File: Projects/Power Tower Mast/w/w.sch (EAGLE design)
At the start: 25 parts

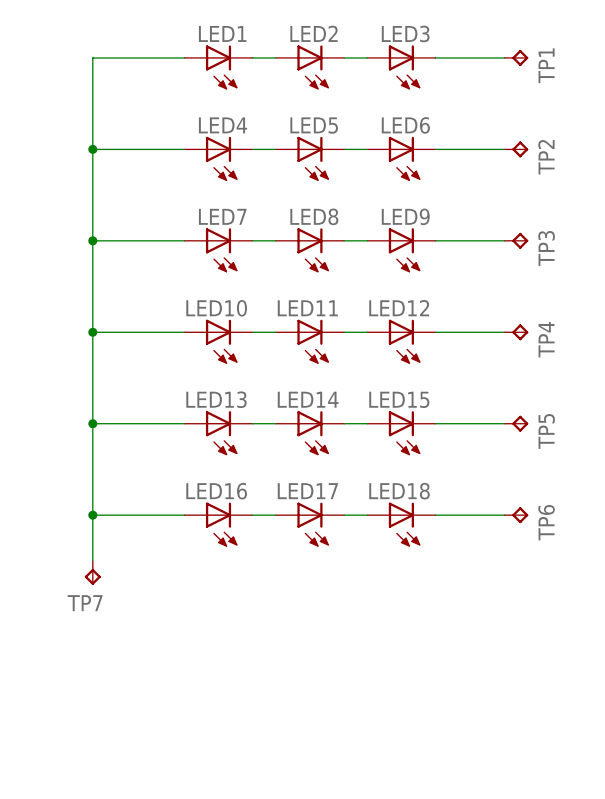
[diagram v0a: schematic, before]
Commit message: updated with extra vias and panelized
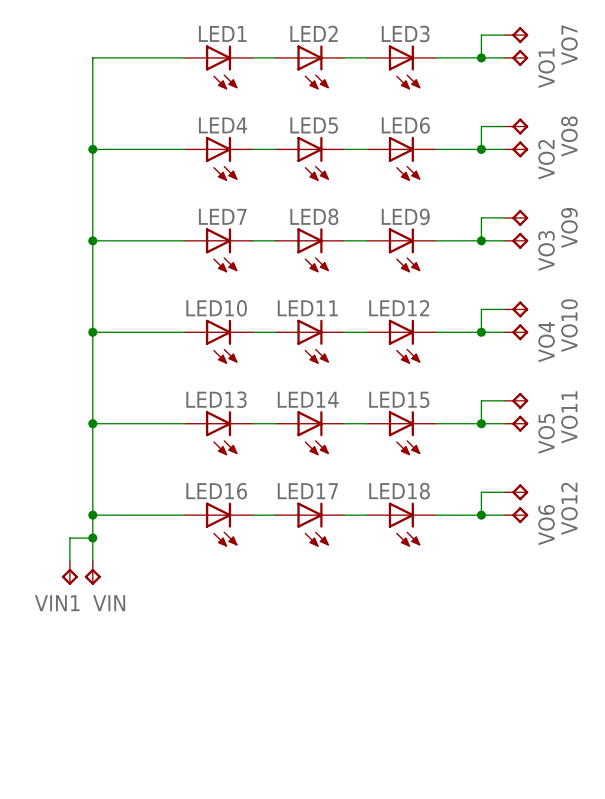
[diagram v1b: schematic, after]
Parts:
- added VIN1, VO10, VO11, VO12, VO7, VO8, VO9: (no value), CyberRailGuru:TEST_POINTPAD1-20
- renumbered TP1 to VO1, TP2 to VO2, TP3 to VO3, TP4 to VO4, TP5 to VO5, TP6 to VO6, TP7 to VIN
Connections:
- removed net VIN3: LED1.A, LED10.A, LED13.A, LED16.A, LED4.A, LED7.A, VIN.TP
- removed net VOUT14: LED3.C, VO1.TP
- removed net VOUT15: LED6.C, VO2.TP
- removed net VOUT16: LED9.C, VO3.TP
- removed net VOUT17: LED12.C, VO4.TP
- removed net VOUT18: LED15.C, VO5.TP
- removed net VOUT19: LED18.C, VO6.TP
- new net VIN: LED1.A, LED10.A, LED13.A, LED16.A, LED4.A, LED7.A, VIN.TP, VIN1.TP
- new net VOUT1: LED3.C, VO1.TP, VO7.TP
- new net VOUT2: LED6.C, VO2.TP, VO8.TP
- new net VOUT3: LED9.C, VO3.TP, VO9.TP
- new net VOUT4: LED12.C, VO10.TP, VO4.TP
- new net VOUT5: LED15.C, VO11.TP, VO5.TP
- new net VOUT6: LED18.C, VO12.TP, VO6.TP

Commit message: fixed ratio for all letters; continued to update layouts
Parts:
- added LED19, LED20, LED21: (no value), CyberRailGuru:LED0805
- added VO13, VO14: (no value), CyberRailGuru:TEST_POINTPAD1-20
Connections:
- new net N$1: LED19.C, LED20.A
- new net N$2: LED20.C, LED21.A
- new net VOUT7: LED21.C, VO14.TP, VO7.TP
- net VIN: now also LED19.A
- net VOUT1: now also VO8.TP; no longer VO7.TP
- net VOUT2: now also VO9.TP; no longer VO8.TP
- net VOUT3: now also VO10.TP; no longer VO9.TP
- net VOUT4: now also VO11.TP; no longer VO10.TP
- net VOUT5: now also VO12.TP; no longer VO11.TP
- net VOUT6: now also VO13.TP; no longer VO12.TP
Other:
- moved on the sheet: VIN, VIN1, VO10, VO11, VO12, VO7, VO8, VO9
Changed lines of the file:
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@@
 <part name="VO6" library="CyberRailGuru" deviceset="TEST_POINT" device="PAD1-20"/>
 <part name="VIN1" library="CyberRailGuru" deviceset="TEST_POINT" device="PAD1-20"/>
-<part name="VO7" library="CyberRailGuru" deviceset="TEST_POINT" device="PAD1-20"/>
 <part name="VO8" library="CyberRailGuru" deviceset="TEST_POINT" device="PAD1-20"/>
 <part name="VO9" library="CyberRailGuru" deviceset="TEST_POINT" device="PAD1-20"/>
@@
 <part name="VO11" library="CyberRailGuru" deviceset="TEST_POINT" device="PAD1-20"/>
 <part name="VO12" library="CyberRailGuru" deviceset="TEST_POINT" device="PAD1-20"/>
+<part name="VO13" library="CyberRailGuru" deviceset="TEST_POINT" device="PAD1-20"/>
+<part name="LED19" library="CyberRailGuru" deviceset="LED" device="0805"/>
+<part name="LED20" library="CyberRailGuru" deviceset="LED" device="0805"/>
+<part name="LED21" library="CyberRailGuru" deviceset="LED" device="0805"/>
+<part name="VO7" library="CyberRailGuru" deviceset="TEST_POINT" device="PAD1-20"/>
+<part name="VO14" library="CyberRailGuru" deviceset="TEST_POINT" device="PAD1-20"/>
 </parts>
 <sheets>
@@
 <instance part="LED17" gate="G$1" x="91.44" y="149.86" rot="R90"/>
 <instance part="LED16" gate="G$1" x="81.28" y="149.86" rot="R90"/>
-<instance part="VIN" gate="G$1" x="68.58" y="142.24" smashed="yes" rot="R180">
-<attribute name="NAME" x="72.39" y="140.97" size="1.778" layer="95" rot="R180"/>
-<attribute name="VALUE" x="67.31" y="143.51" size="1.778" layer="96" rot="R180"/>
+<instance part="VIN" gate="G$1" x="68.58" y="124.46" smashed="yes" rot="R180">
+<attribute name="NAME" x="72.39" y="123.19" size="1.778" layer="95" rot="R180"/>
+<attribute name="VALUE" x="67.31" y="125.73" size="1.778" layer="96" rot="R180"/>
 </instance>
 <instance part="VO1" gate="G$1" x="116.84" y="200.66" smashed="yes" rot="R270">
@@
 <attribute name="VALUE" x="115.57" y="148.59" size="1.778" layer="96" rot="R270"/>
 </instance>
-<instance part="VIN1" gate="G$1" x="66.04" y="142.24" smashed="yes" rot="R180">
-<attribute name="NAME" x="67.31" y="140.97" size="1.778" layer="95" rot="R180"/>
-<attribute name="VALUE" x="64.77" y="143.51" size="1.778" layer="96" rot="R180"/>
-</instance>
-<instance part="VO7" gate="G$1" x="116.84" y="203.2" smashed="yes" rot="R270">
+<instance part="VIN1" gate="G$1" x="66.04" y="124.46" smashed="yes" rot="R180">
+<attribute name="NAME" x="67.31" y="123.19" size="1.778" layer="95" rot="R180"/>
+<attribute name="VALUE" x="64.77" y="125.73" size="1.778" layer="96" rot="R180"/>
+</instance>
+<instance part="VO8" gate="G$1" x="116.84" y="203.2" smashed="yes" rot="R270">
 <attribute name="NAME" x="120.65" y="204.47" size="1.778" layer="95" rot="R270"/>
 <attribute name="VALUE" x="115.57" y="201.93" size="1.778" layer="96" rot="R270"/>
 </instance>
-<instance part="VO8" gate="G$1" x="116.84" y="193.04" smashed="yes" rot="R270">
+<instance part="VO9" gate="G$1" x="116.84" y="193.04" smashed="yes" rot="R270">
 <attribute name="NAME" x="120.65" y="194.31" size="1.778" layer="95" rot="R270"/>
 <attribute name="VALUE" x="115.57" y="191.77" size="1.778" layer="96" rot="R270"/>
 </instance>
-<instance part="VO9" gate="G$1" x="116.84" y="182.88" smashed="yes" rot="R270">
+<instance part="VO10" gate="G$1" x="116.84" y="182.88" smashed="yes" rot="R270">
 <attribute name="NAME" x="120.65" y="184.15" size="1.778" layer="95" rot="R270"/>
 <attribute name="VALUE" x="115.57" y="181.61" size="1.778" layer="96" rot="R270"/>
 </instance>
-<instance part="VO10" gate="G$1" x="116.84" y="172.72" smashed="yes" rot="R270">
+<instance part="VO11" gate="G$1" x="116.84" y="172.72" smashed="yes" rot="R270">
 <attribute name="NAME" x="120.65" y="173.99" size="1.778" layer="95" rot="R270"/>
 <attribute name="VALUE" x="115.57" y="171.45" size="1.778" layer="96" rot="R270"/>
 </instance>
-<instance part="VO11" gate="G$1" x="116.84" y="162.56" smashed="yes" rot="R270">
+<instance part="VO12" gate="G$1" x="116.84" y="162.56" smashed="yes" rot="R270">
 <attribute name="NAME" x="120.65" y="163.83" size="1.778" layer="95" rot="R270"/>
 <attribute name="VALUE" x="115.57" y="161.29" size="1.778" layer="96" rot="R270"/>
 </instance>
-<instance part="VO12" gate="G$1" x="116.84" y="152.4" smashed="yes" rot="R270">
+<instance part="VO13" gate="G$1" x="116.84" y="152.4" smashed="yes" rot="R270">
 <attribute name="NAME" x="120.65" y="153.67" size="1.778" layer="95" rot="R270"/>
 <attribute name="VALUE" x="115.57" y="151.13" size="1.778" layer="96" rot="R270"/>
+</instance>
+<instance part="LED19" gate="G$1" x="81.28" y="139.7" rot="R90"/>
+<instance part="LED20" gate="G$1" x="91.44" y="139.7" rot="R90"/>
+<instance part="LED21" gate="G$1" x="101.6" y="139.7" rot="R90"/>
+<instance part="VO7" gate="G$1" x="116.84" y="139.7" smashed="yes" rot="R270">
+<attribute name="NAME" x="118.11" y="140.97" size="1.778" layer="95" rot="R270"/>
+<attribute name="VALUE" x="115.57" y="138.43" size="1.778" layer="96" rot="R270"/>
+</instance>
+<instance part="VO14" gate="G$1" x="116.84" y="142.24" smashed="yes" rot="R270">
+<attribute name="NAME" x="120.65" y="143.51" size="1.778" layer="95" rot="R270"/>
+<attribute name="VALUE" x="115.57" y="140.97" size="1.778" layer="96" rot="R270"/>
 </instance>
 </instances>
@@
 <wire x1="106.68" y1="200.66" x2="111.76" y2="200.66" width="0.1524" layer="91"/>
 <pinref part="VO1" gate="G$1" pin="TP"/>
-<pinref part="VO7" gate="G$1" pin="TP"/>
+<pinref part="VO8" gate="G$1" pin="TP"/>
 <wire x1="111.76" y1="200.66" x2="114.3" y2="200.66" width="0.1524" layer="91"/>
 <wire x1="114.3" y1="203.2" x2="111.76" y2="203.2" width="0.1524" layer="91"/>
@@
 <wire x1="106.68" y1="190.5" x2="111.76" y2="190.5" width="0.1524" layer="91"/>
 <pinref part="VO2" gate="G$1" pin="TP"/>
-<pinref part="VO8" gate="G$1" pin="TP"/>
+<pinref part="VO9" gate="G$1" pin="TP"/>
 <wire x1="111.76" y1="190.5" x2="114.3" y2="190.5" width="0.1524" layer="91"/>
 <wire x1="114.3" y1="193.04" x2="111.76" y2="193.04" width="0.1524" layer="91"/>
@@
 <wire x1="106.68" y1="180.34" x2="111.76" y2="180.34" width="0.1524" layer="91"/>
 <pinref part="VO3" gate="G$1" pin="TP"/>
-<pinref part="VO9" gate="G$1" pin="TP"/>
+<pinref part="VO10" gate="G$1" pin="TP"/>
 <wire x1="111.76" y1="180.34" x2="114.3" y2="180.34" width="0.1524" layer="91"/>
 <wire x1="114.3" y1="182.88" x2="111.76" y2="182.88" width="0.1524" layer="91"/>
@@
 <wire x1="106.68" y1="170.18" x2="111.76" y2="170.18" width="0.1524" layer="91"/>
 <pinref part="VO4" gate="G$1" pin="TP"/>
-<pinref part="VO10" gate="G$1" pin="TP"/>
+<pinref part="VO11" gate="G$1" pin="TP"/>
 <wire x1="111.76" y1="170.18" x2="114.3" y2="170.18" width="0.1524" layer="91"/>
 <wire x1="114.3" y1="172.72" x2="111.76" y2="172.72" width="0.1524" layer="91"/>
@@
 <wire x1="106.68" y1="160.02" x2="111.76" y2="160.02" width="0.1524" layer="91"/>
 <pinref part="VO5" gate="G$1" pin="TP"/>
-<pinref part="VO11" gate="G$1" pin="TP"/>
+<pinref part="VO12" gate="G$1" pin="TP"/>
 <wire x1="111.76" y1="160.02" x2="114.3" y2="160.02" width="0.1524" layer="91"/>
 <wire x1="114.3" y1="162.56" x2="111.76" y2="162.56" width="0.1524" layer="91"/>
@@
 <wire x1="106.68" y1="149.86" x2="111.76" y2="149.86" width="0.1524" layer="91"/>
 <pinref part="VO6" gate="G$1" pin="TP"/>
-<pinref part="VO12" gate="G$1" pin="TP"/>
+<pinref part="VO13" gate="G$1" pin="TP"/>
 <wire x1="111.76" y1="149.86" x2="114.3" y2="149.86" width="0.1524" layer="91"/>
 <wire x1="114.3" y1="152.4" x2="111.76" y2="152.4" width="0.1524" layer="91"/>
@@
 <wire x1="68.58" y1="170.18" x2="68.58" y2="160.02" width="0.1524" layer="91"/>
 <wire x1="68.58" y1="160.02" x2="68.58" y2="149.86" width="0.1524" layer="91"/>
-<wire x1="68.58" y1="149.86" x2="68.58" y2="147.32" width="0.1524" layer="91"/>
 <pinref part="LED16" gate="G$1" pin="A"/>
-<wire x1="68.58" y1="147.32" x2="68.58" y2="144.78" width="0.1524" layer="91"/>
+<wire x1="68.58" y1="149.86" x2="68.58" y2="139.7" width="0.1524" layer="91"/>
+<wire x1="68.58" y1="139.7" x2="68.58" y2="129.54" width="0.1524" layer="91"/>
+<wire x1="68.58" y1="129.54" x2="68.58" y2="127" width="0.1524" layer="91"/>
 <wire x1="68.58" y1="149.86" x2="78.74" y2="149.86" width="0.1524" layer="91"/>
 <pinref part="LED13" gate="G$1" pin="A"/>
@@
 <pinref part="VIN" gate="G$1" pin="TP"/>
 <pinref part="VIN1" gate="G$1" pin="TP"/>
-<wire x1="66.04" y1="144.78" x2="66.04" y2="147.32" width="0.1524" layer="91"/>
-<wire x1="66.04" y1="147.32" x2="68.58" y2="147.32" width="0.1524" layer="91"/>
-<junction x="68.58" y="147.32"/>
-</segment>
-</net>
+<wire x1="66.04" y1="127" x2="66.04" y2="129.54" width="0.1524" layer="91"/>
+<wire x1="66.04" y1="129.54" x2="68.58" y2="129.54" width="0.1524" layer="91"/>
+<junction x="68.58" y="129.54"/>
+<pinref part="LED19" gate="G$1" pin="A"/>
+<wire x1="78.74" y1="139.7" x2="68.58" y2="139.7" width="0.1524" layer="91"/>
+<junction x="68.58" y="139.7"/>
+</segment>
+</net>
+<net name="VOUT7" class="0">
+<segment>
+<pinref part="VO7" gate="G$1" pin="TP"/>
+<pinref part="VO14" gate="G$1" pin="TP"/>
+<wire x1="111.76" y1="139.7" x2="114.3" y2="139.7" width="0.1524" layer="91"/>
+<wire x1="114.3" y1="142.24" x2="111.76" y2="142.24" width="0.1524" layer="91"/>
+<wire x1="111.76" y1="142.24" x2="111.76" y2="139.7" width="0.1524" layer="91"/>
+<pinref part="LED21" gate="G$1" pin="C"/>
+<wire x1="106.68" y1="139.7" x2="111.76" y2="139.7" width="0.1524" layer="91"/>
+<junction x="111.76" y="139.7"/>
+</segment>
+</net>
+<net name="N$1" class="0">
+<segment>
+<pinref part="LED20" gate="G$1" pin="A"/>
+<pinref part="LED19" gate="G$1" pin="C"/>
+<wire x1="88.9" y1="139.7" x2="86.36" y2="139.7" width="0.1524" layer="91"/>
+</segment>
+</net>
+<net name="N$2" class="0">
+<segment>
+<pinref part="LED21" gate="G$1" pin="A"/>
+<pinref part="LED20" gate="G$1" pin="C"/>
+<wire x1="99.06" y1="139.7" x2="96.52" y2="139.7" width="0.1524" layer="91"/>
+</segment>
+</net>
